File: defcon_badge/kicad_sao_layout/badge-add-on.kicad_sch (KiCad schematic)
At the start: 9 parts

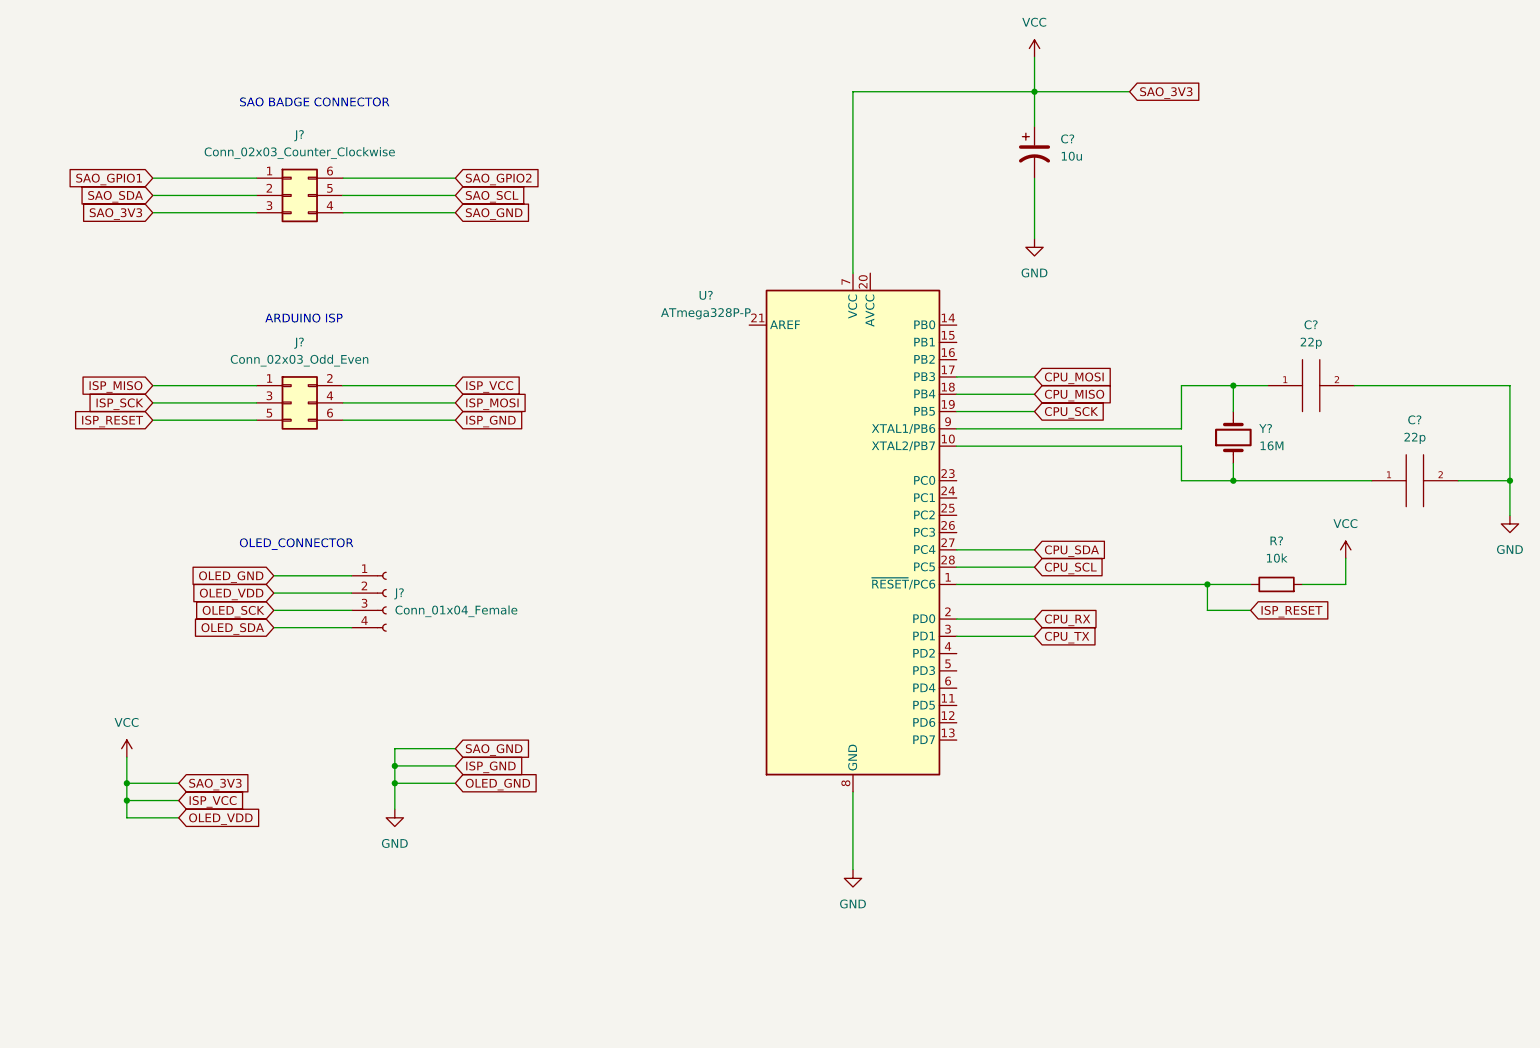
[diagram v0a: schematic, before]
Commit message: Finished badge add on hardware design and sent gerbers to PCB fab
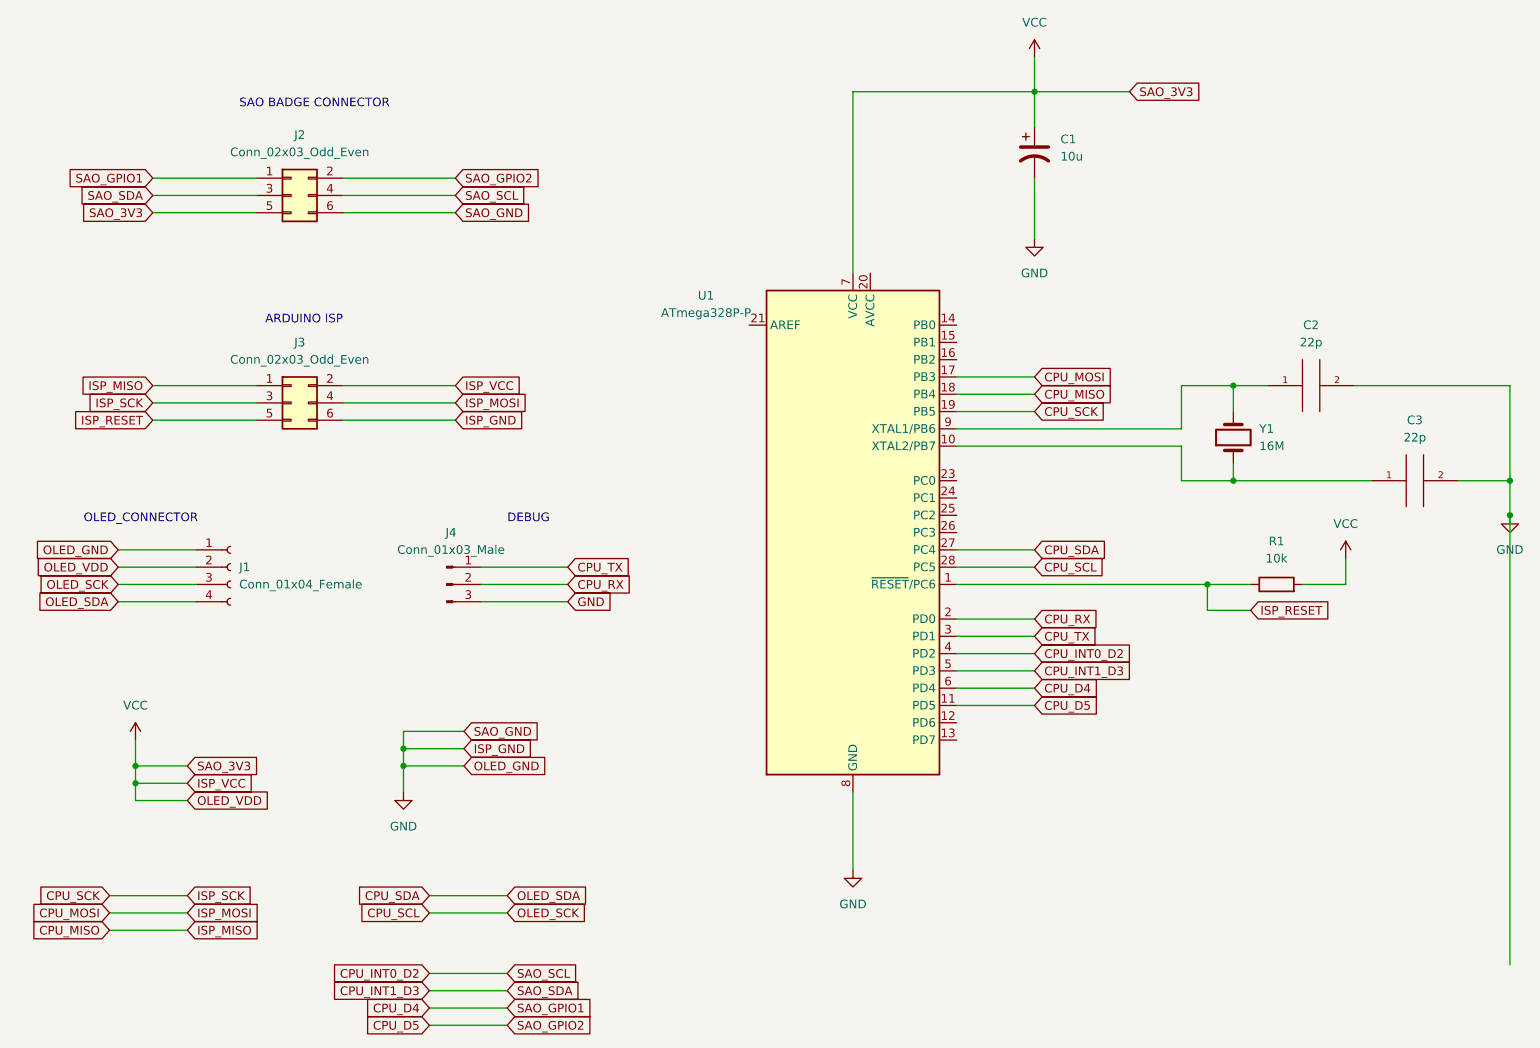
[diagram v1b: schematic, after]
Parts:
- removed J?: Conn_02x03_Counter_Clockwise, symbol Connector_Generic:Conn_02x03_Counter_Clockwise
- added J2: Conn_02x03_Odd_Even, Connector_PinSocket_2.54mm:PinSocket_2x03_P2.54mm_Vertical, symbol Connector_Generic:Conn_02x03_Odd_Even
- added J4: Conn_01x03_Male, Connector_PinSocket_2.54mm:PinSocket_1x03_P2.54mm_Vertical, symbol Connector:Conn_01x03_Male
- C1: renamed from C?; footprint (none) -> Capacitor_THT:CP_Radial_D5.0mm_P2.50mm
- C2, C3: renamed from C?; footprint (none) -> Capacitor_THT:C_Disc_D5.1mm_W3.2mm_P5.00mm
- J1: renamed from J?; footprint (none) -> Connector_PinSocket_2.54mm:PinSocket_1x04_P2.54mm_Vertical
- J3: renamed from J?; footprint (none) -> Connector_PinSocket_2.54mm:PinSocket_2x03_P2.54mm_Vertical
- R1: renamed from R?; footprint (none) -> Resistor_THT:R_Axial_DIN0207_L6.3mm_D2.5mm_P15.24mm_Horizontal
- Y1: renamed from Y?; footprint (none) -> Crystal:Resonator-2Pin_W10.0mm_H5.0mm
- gave numbers to parts that had none: 1
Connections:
- net ISP_MISO is gone; now on net CPU_MISO: J3.1 (Pin_1)
- net ISP_MOSI is gone; now on net CPU_MOSI: J3.4 (Pin_4)
- net ISP_SCK is gone; now on net CPU_SCK: J3.3 (Pin_3)
- net OLED_SCK is gone; now on net CPU_SCL: J1.3 (Pin_3)
- net OLED_SDA is gone; now on net CPU_SDA: J1.4 (Pin_4)
- net CPU_RX: now also J4.2 (Pin_2)
- net CPU_TX: now also J4.1 (Pin_1)
- net GND: now also J2.6 (Pin_6), J4.3 (Pin_3)
- net VCC: now also J2.5 (Pin_5)
- net CPU_D5: now reaches U1.11 (PD5)
- net CPU_D5: now also J2.2 (Pin_2)
- net CPU_INT0_D2: now reaches U1.4 (PD2)
- net CPU_INT0_D2: now also J2.4 (Pin_4)
- net CPU_INT1_D3: now reaches U1.5 (PD3)
- net CPU_INT1_D3: now also J2.3 (Pin_3)
- net CPU_D4: now reaches U1.6 (PD4)
- net CPU_D4: now also J2.1 (Pin_1)
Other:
- note added: "DEBUG"
- moved on the sheet: J1
